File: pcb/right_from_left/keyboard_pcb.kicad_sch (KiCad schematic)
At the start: 42 parts, among them J1 TRRS, K0 KEYSW, K1 KEYSW, K10 KEYSW, K11 KEYSW, K12 KEYSW, K13 KEYSW, K14 KEYSW, K15 KEYSW, K2 KEYSW, K20 KEYSW, K21 KEYSW, K22 KEYSW, K23 KEYSW, K24 KEYSW, K25 KEYSW, K3 KEYSW, K30 KEYSW, K31 KEYSW, K32 KEYSW, K4 KEYSW, K5 KEYSW, U1 MCP23009-E/SO, U2 Pico

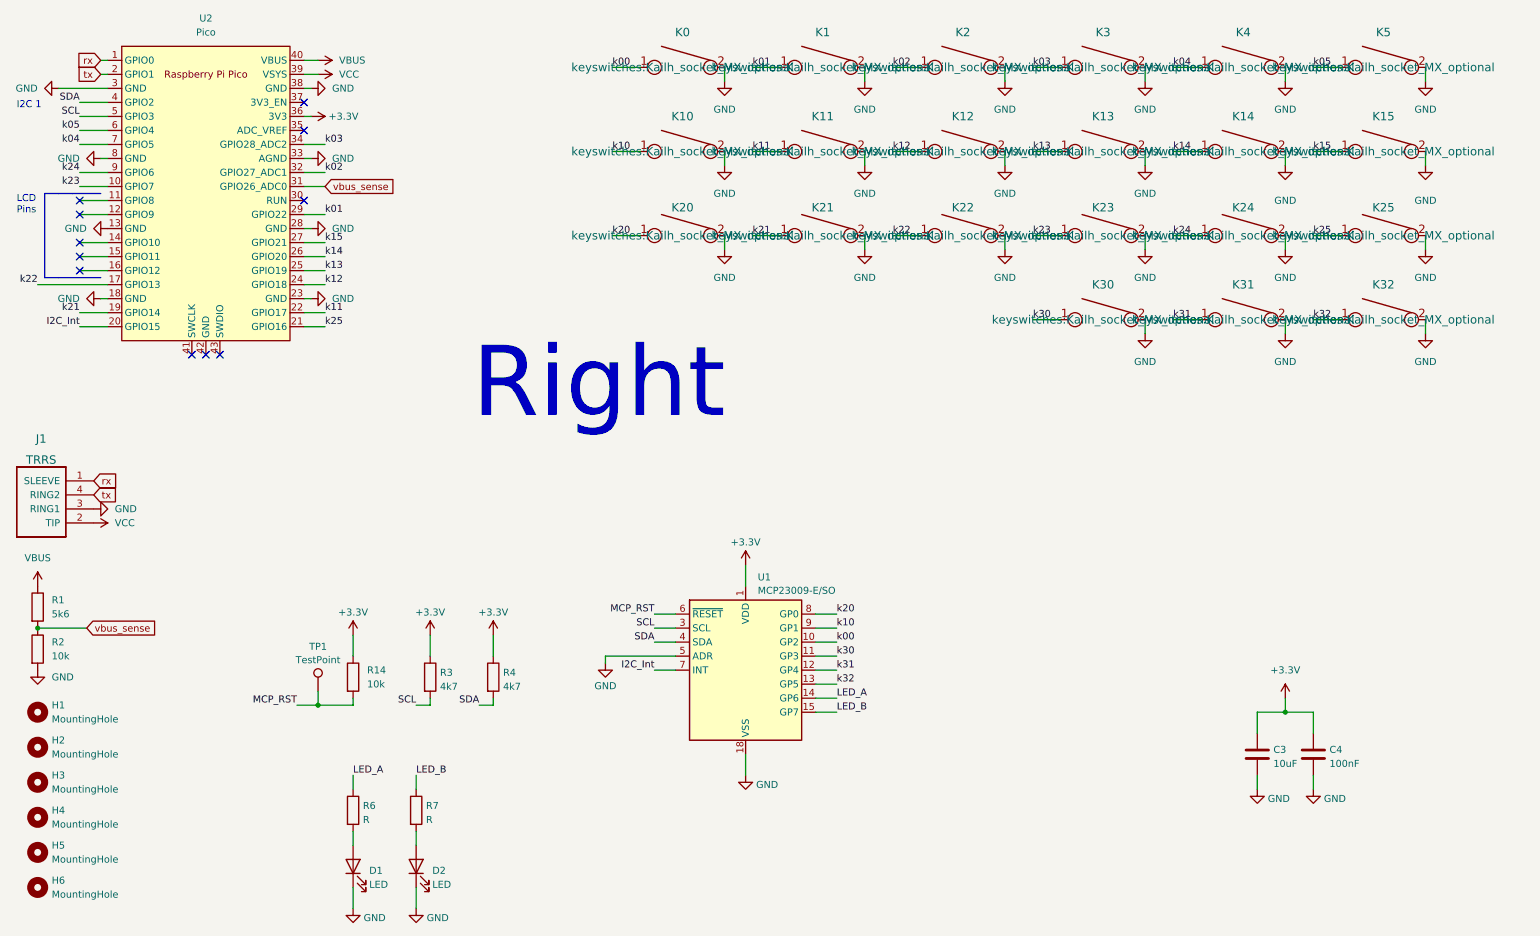
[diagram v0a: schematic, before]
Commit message: Revision 1.1 -RFR- right pcb layout fix added Standoff PN
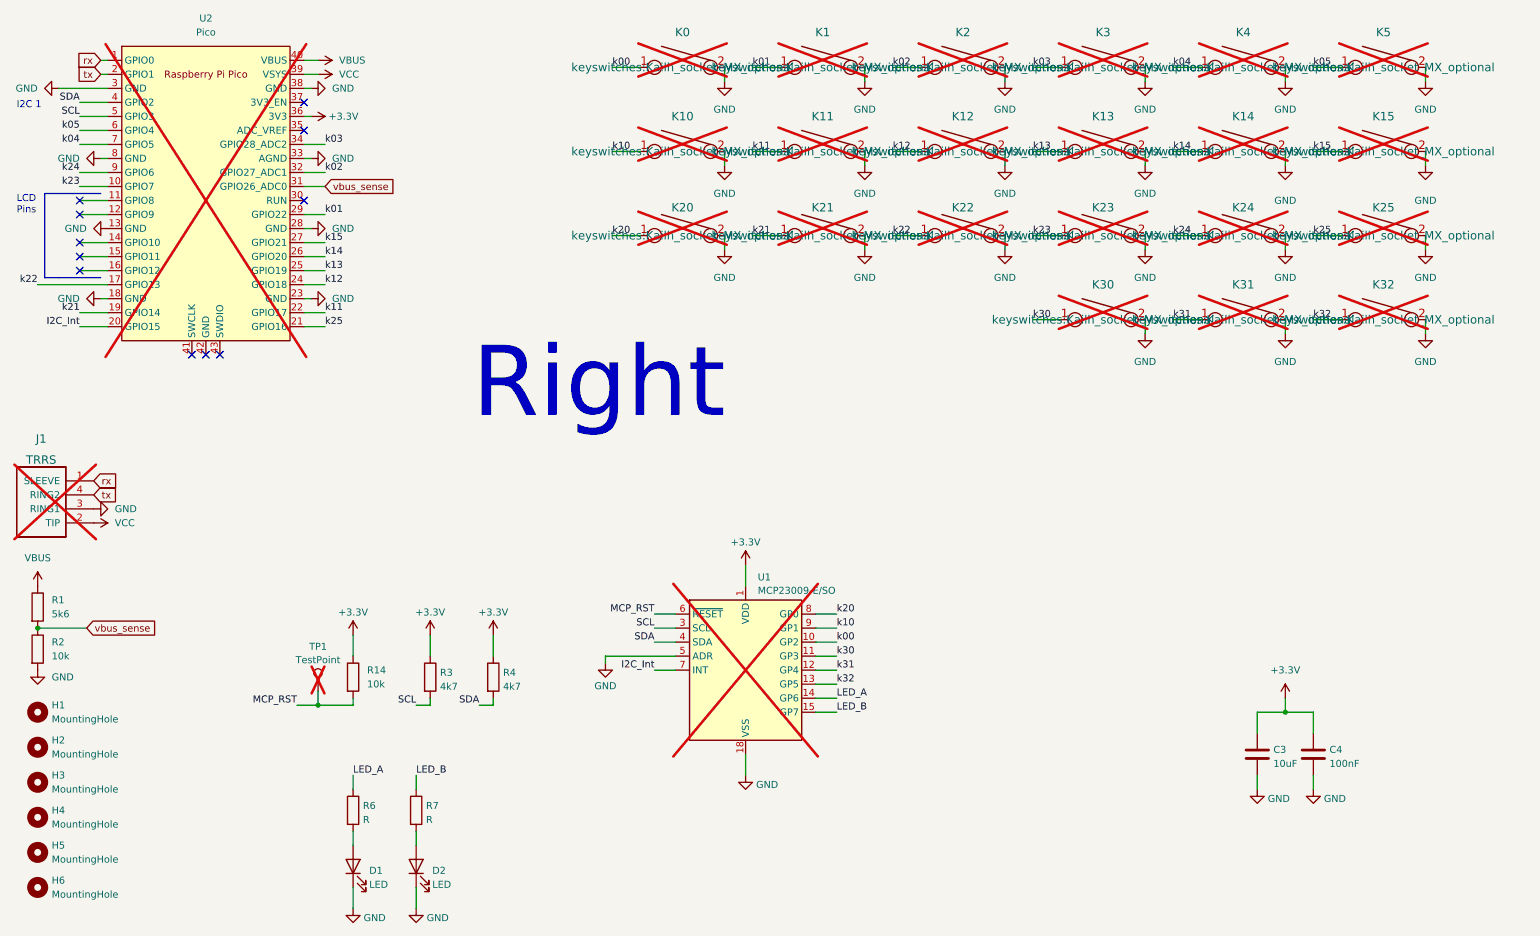
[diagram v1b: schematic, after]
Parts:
- J1, K0, K1, K10, K11, K12, K13, K14, K15, K2, K20, K21, K22, K23, K24, K25, K3, K30, K31, K32, K4, K5, TP1, U1, U2: now not fitted
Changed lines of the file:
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@@
 		(in_bom yes)
 		(on_board yes)
-		(dnp no)
+		(dnp yes)
 		(fields_autoplaced yes)
 		(property "Reference" "K32"
@@
 		(in_bom yes)
 		(on_board yes)
-		(dnp no)
+		(dnp yes)
 		(fields_autoplaced yes)
 		(property "Reference" "TP1"
@@
 		(in_bom yes)
 		(on_board yes)
-		(dnp no)
+		(dnp yes)
 		(fields_autoplaced yes)
 		(property "Reference" "U1"
@@
 		(in_bom yes)
 		(on_board yes)
-		(dnp no)
+		(dnp yes)
 		(property "Reference" "K24"
 			(at 238.76 55.88 0)
@@
 		(in_bom yes)
 		(on_board yes)
-		(dnp no)
+		(dnp yes)
 		(fields_autoplaced yes)
 		(property "Reference" "K0"
@@
 			)
 		)
-		(property "Description" ""
+		(property "Description" "https://www.we-online.com/en/components/products/SMSI_SMT_STEEL_SPACER_M2_5_THREAD_INTERNAL#9774020151R"
 			(at 20.32 166.37 0)
 			(effects
@@
 		(in_bom yes)
 		(on_board yes)
-		(dnp no)
+		(dnp yes)
 		(fields_autoplaced yes)
 		(property "Reference" "K15"
@@
 			)
 		)
-		(property "Description" ""
+		(property "Description" "https://www.we-online.com/en/components/products/SMSI_SMT_STEEL_SPACER_M2_5_THREAD_INTERNAL#9774020151R"
 			(at 20.32 153.67 0)
 			(effects
@@
 		(in_bom yes)
 		(on_board yes)
-		(dnp no)
+		(dnp yes)
 		(fields_autoplaced yes)
 		(property "Reference" "K3"
@@
 		(in_bom yes)
 		(on_board yes)
-		(dnp no)
+		(dnp yes)
 		(fields_autoplaced yes)
 		(property "Reference" "K2"
@@
 		(in_bom yes)
 		(on_board yes)
-		(dnp no)
+		(dnp yes)
 		(fields_autoplaced yes)
 		(property "Reference" "K11"
@@
 		(in_bom yes)
 		(on_board yes)
-		(dnp no)
+		(dnp yes)
 		(property "Reference" "K22"
 			(at 187.96 55.88 0)
@@
 		(in_bom yes)
 		(on_board yes)
-		(dnp no)
+		(dnp yes)
 		(fields_autoplaced yes)
 		(property "Reference" "K4"
@@
 		(in_bom yes)
 		(on_board yes)
-		(dnp no)
+		(dnp yes)
 		(fields_autoplaced yes)
 		(property "Reference" "K30"
@@
 		(in_bom yes)
 		(on_board yes)
-		(dnp no)
+		(dnp yes)
 		(fields_autoplaced yes)
 		(property "Reference" "J1"
@@
 		(in_bom yes)
 		(on_board yes)
-		(dnp no)
+		(dnp yes)
 		(fields_autoplaced yes)
 		(property "Reference" "U2"
@@
 		(in_bom yes)
 		(on_board yes)
-		(dnp no)
+		(dnp yes)
 		(property "Reference" "K20"
 			(at 137.16 55.88 0)
@@
 		(in_bom yes)
 		(on_board yes)
-		(dnp no)
+		(dnp yes)
 		(property "Reference" "K23"
 			(at 213.36 55.88 0)
@@
 		(in_bom yes)
 		(on_board yes)
-		(dnp no)
+		(dnp yes)
 		(fields_autoplaced yes)
 		(property "Reference" "K10"
@@
 		(in_bom yes)
 		(on_board yes)
-		(dnp no)
+		(dnp yes)
 		(property "Reference" "K1"
 			(at 162.56 24.13 0)
@@
 		(in_bom yes)
 		(on_board yes)
-		(dnp no)
+		(dnp yes)
 		(property "Reference" "K25"
 			(at 264.16 55.88 0)
@@
 		(in_bom yes)
 		(on_board yes)
-		(dnp no)
+		(dnp yes)
 		(fields_autoplaced yes)
 		(property "Reference" "K31"
@@
 			)
 		)
-		(property "Description" ""
+		(property "Description" "https://www.we-online.com/en/components/products/SMSI_SMT_STEEL_SPACER_M2_5_THREAD_INTERNAL#9774020151R"
 			(at 20.32 160.02 0)
 			(effects
@@
 		(in_bom yes)
 		(on_board yes)
-		(dnp no)
+		(dnp yes)
 		(fields_autoplaced yes)
 		(property "Reference" "K14"
@@
 		(in_bom yes)
 		(on_board yes)
-		(dnp no)
+		(dnp yes)
 		(fields_autoplaced yes)
 		(property "Reference" "K13"
@@
 		(in_bom yes)
 		(on_board yes)
-		(dnp no)
+		(dnp yes)
 		(property "Reference" "K21"
 			(at 162.56 55.88 0)
@@
 		(in_bom yes)
 		(on_board yes)
-		(dnp no)
+		(dnp yes)
 		(fields_autoplaced yes)
 		(property "Reference" "K12"
@@
 			)
 		)
-		(property "Description" ""
+		(property "Description" "https://www.we-online.com/en/components/products/SMSI_SMT_STEEL_SPACER_M2_5_THREAD_INTERNAL#9774020151R"
 			(at 20.32 172.72 0)
 			(effects
@@
 			)
 		)
-		(property "Description" ""
+		(property "Description" "https://www.we-online.com/en/components/products/SMSI_SMT_STEEL_SPACER_M2_5_THREAD_INTERNAL#9774020151R"
 			(at 20.32 147.32 0)
 			(effects
@@
 			)
 		)
-		(property "Description" ""
+		(property "Description" "https://www.we-online.com/en/components/products/SMSI_SMT_STEEL_SPACER_M2_5_THREAD_INTERNAL#9774020151R"
 			(at 20.32 179.07 0)
 			(effects
@@
 		(in_bom yes)
 		(on_board yes)
-		(dnp no)
+		(dnp yes)
 		(fields_autoplaced yes)
 		(property "Reference" "K5"
